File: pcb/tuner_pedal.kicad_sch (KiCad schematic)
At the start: 67 parts, among them J1 SWD, J2 Fermion 1.8" TFT LCD, J3 UART, J4 Potentiometer, SW1 SW_Push, SW2 SW_Push, U1 STM32F411CEUx, U2 PCM1802DB, U3 MCP1700T-3302E/TT, U4 TPS54302, X1 ECS-2520MVLC-081.92, Y1 25MHz 9pF

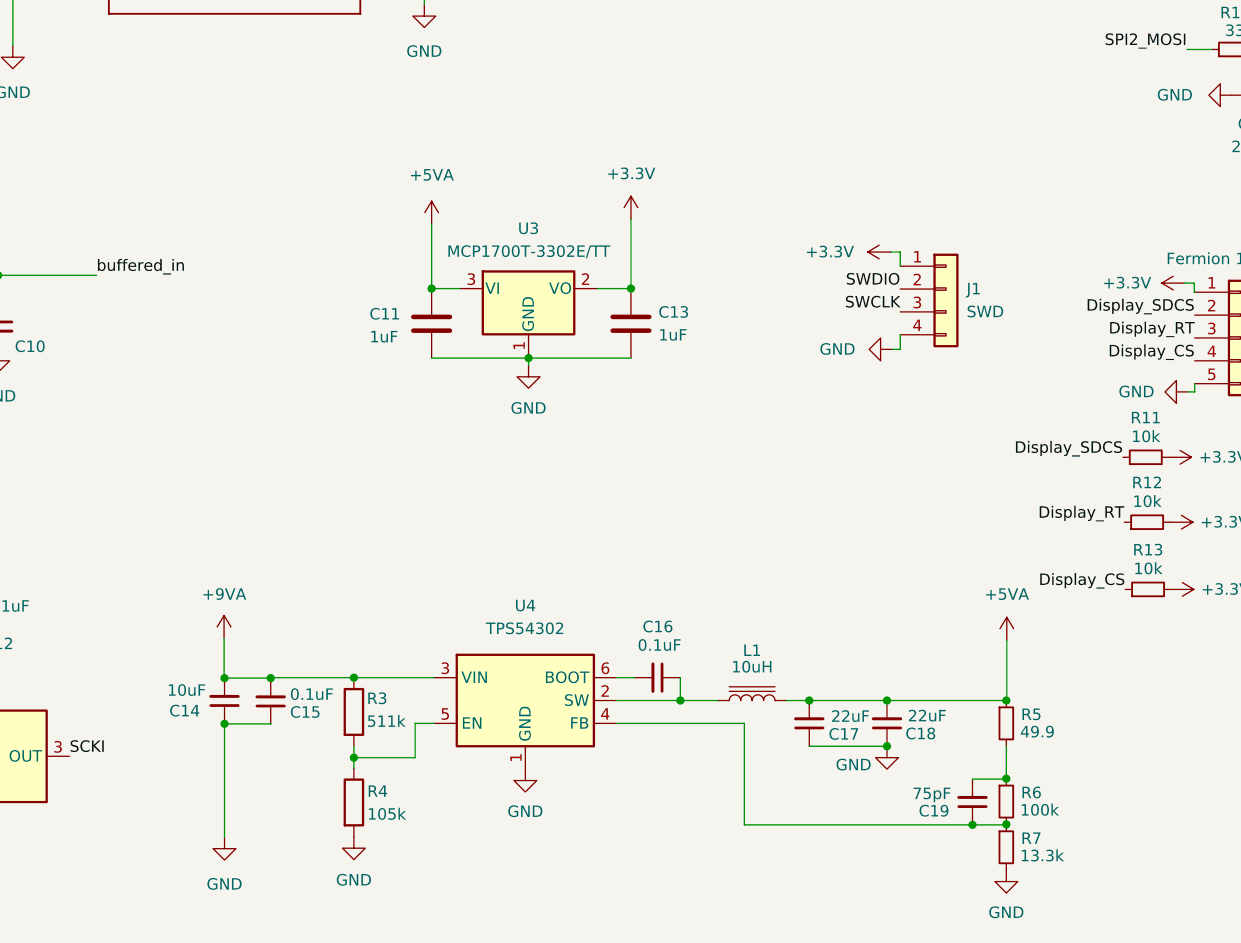
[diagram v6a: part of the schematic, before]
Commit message: Created a power sheet
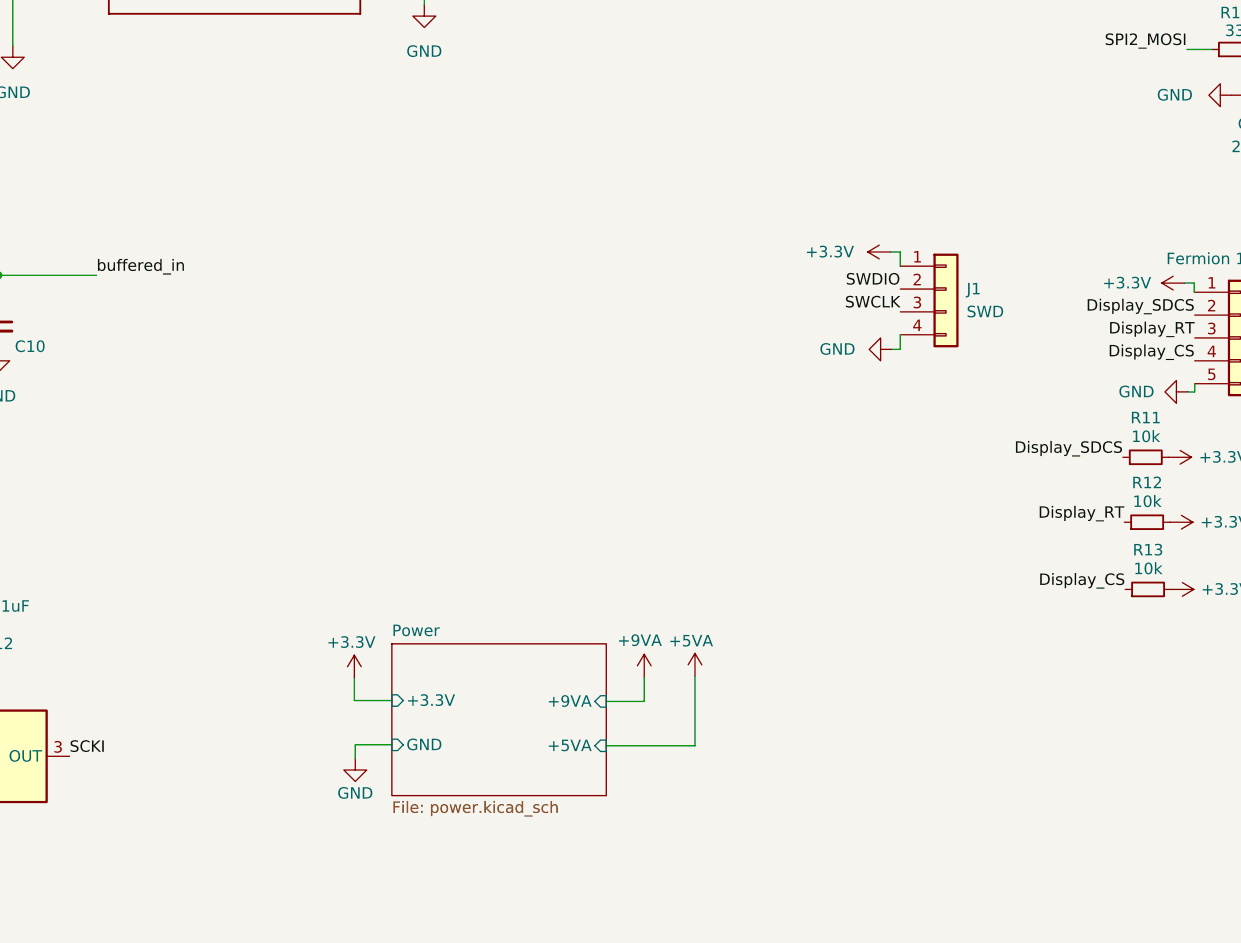
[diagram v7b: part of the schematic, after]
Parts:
- removed C11, C13: 1uF, symbol Device:C
- removed C14: 10uF, symbol Device:C_Small
- removed C15, C16: 0.1uF, symbol Device:C_Small
- removed C17, C18: 22uF, symbol Device:C_Small
- removed C19: 75pF, symbol Device:C_Small
- removed L1: 10uH, symbol Device:L_Iron
- removed R3: 511k, symbol Device:R
- removed R4: 105k, symbol Device:R
- removed R5: 49.9, symbol Device:R_Small
- removed R6: 100k, symbol Device:R_Small
- removed R7: 13.3k, symbol Device:R_Small
- removed U3: MCP1700T-3302E/TT, Package_TO_SOT_SMD:SOT-23-3, symbol Regulator_Linear:MCP1700x-330xxTT
- removed U4: TPS54302, Package_TO_SOT_SMD:SOT-23-6, symbol Regulator_Switching:TPS54302
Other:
- added sheet Power (power.kicad_sch)

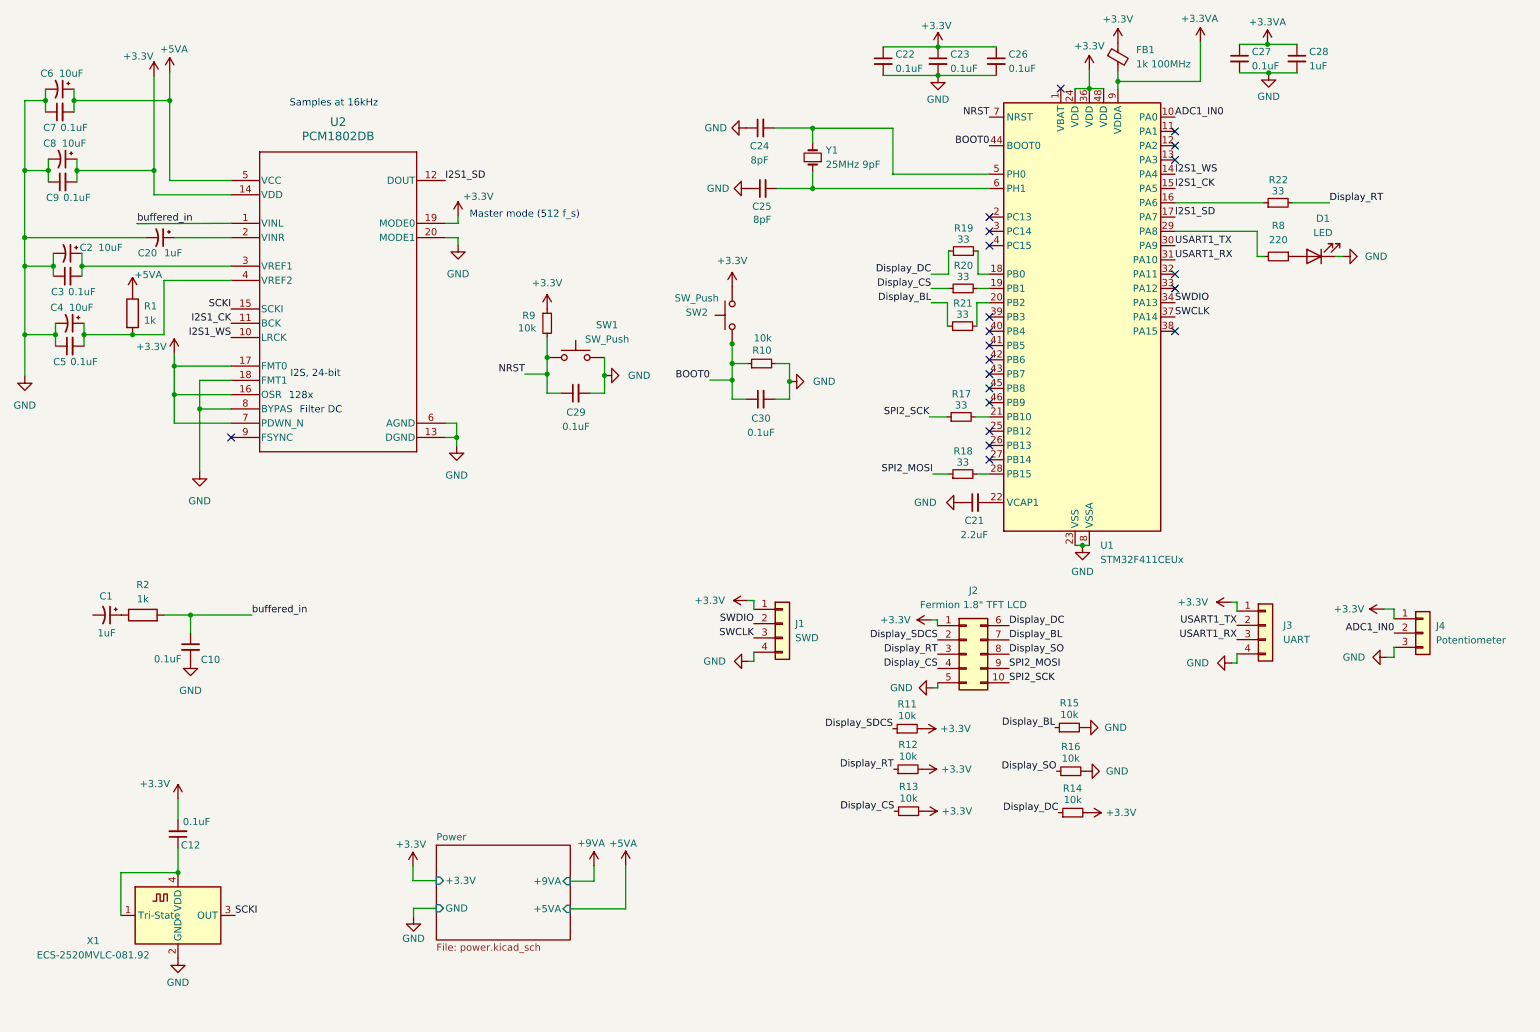
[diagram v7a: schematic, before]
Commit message: Made sheet for ADC
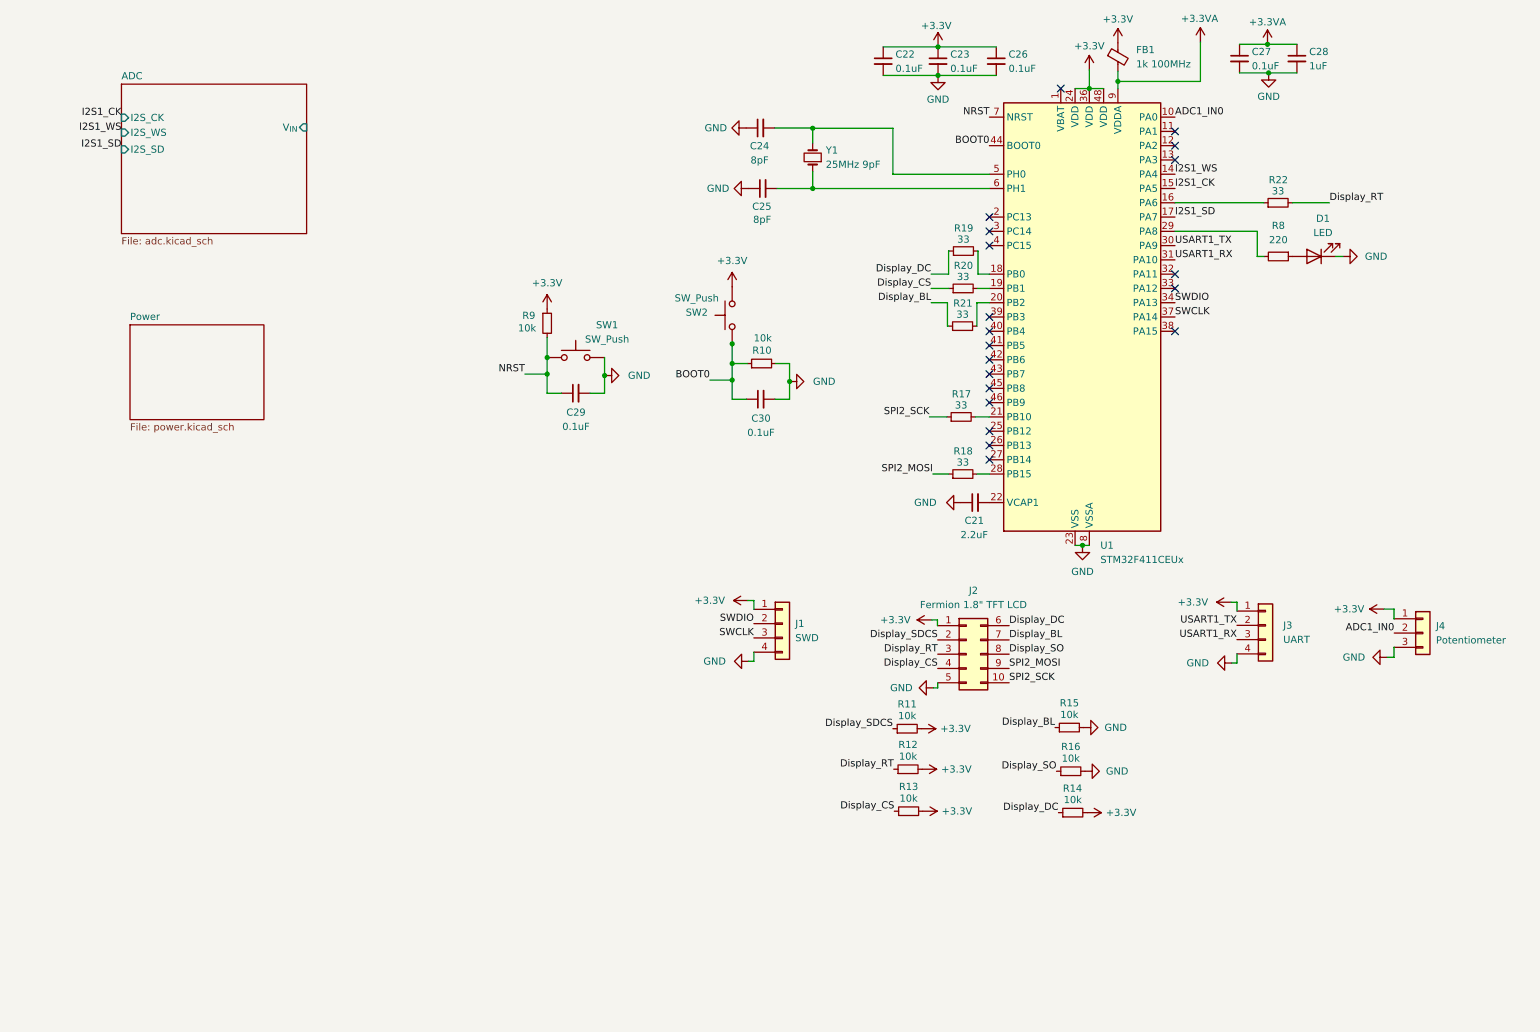
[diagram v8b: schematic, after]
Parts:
- removed C1, C20: 1uF, symbol Device:C_Polarized_Small_US
- removed C10, C12, C3, C5, C7, C9: 0.1uF, symbol Device:C_Small
- removed C2, C4, C6, C8: 10uF, symbol Device:C_Polarized_Small_US
- removed R1, R2: 1k, symbol Device:R
- removed U2: PCM1802DB, pcm1802:DB0020A-IPC_A, symbol pcm1802:PCM1802DB
- removed X1: ECS-2520MVLC-081.92, Oscillator:Oscillator_SMD_ECS_2520MV-xxx-xx-4Pin_2.5x2.0mm, symbol Oscillator:ECS-2520MV-xxx-xx
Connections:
- no-connect marks 21 -> 20
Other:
- added sheet ADC (adc.kicad_sch)
- sheet Power ports: added none; removed +3.3V, +5VA, +9VA, GND
- note removed: "128x"
- note removed: "Filter DC"
- note removed: "I2S, 24-bit"
- note removed: "Master mode (512 f_s)"
- note removed: "Samples at 16kHz"
